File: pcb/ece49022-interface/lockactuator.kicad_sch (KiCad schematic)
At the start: 3 parts

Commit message: start pcb
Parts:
- MOSFET1: footprint SOT23_DMN3200U_2P9X1P3_DIO -> 49022_Footprints:SOT23_DMN3200U_2P9X1P3_DIO-L
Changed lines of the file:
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@@
 			)
 		)
-		(property "Footprint" "SOT23_DMN3200U_2P9X1P3_DIO"
+		(property "Footprint" "49022_Footprints:SOT23_DMN3200U_2P9X1P3_DIO-L"
 			(at 74.93 73.66 0)
 			(effects

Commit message: lock state
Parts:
- added L3: MSS1048T-563ML, symbol ECE49022_Symbols:MSS1048-103MLC
- added R11: R_US, symbol Device:R_US
- added R14: R_close, symbol Device:R_US
- added R7, R8: 10K, 1%, Resistor_SMD:R_0402_1005Metric_Pad0.72x0.64mm_HandSolder, symbol Device:R_US
- added SW2: SW_DPST_x2, symbol Switch:SW_DPST_x2
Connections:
- net +12V: now also R11.1
- net GND: now also R8.2
- net LOAD_RTN: now also L3.2
- new net: L3.1, R11.2
- new net: R14.1, SW2.2 (B)
- new net LOCK_GPIO_STATUS: R7.2, R8.1
- new net LOCK_STATUS: R14.2, R7.1
- new net LOCK_STATUS_VDD: SW2.1 (A)
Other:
- note added: "Equivalent Lock Circuit"
- moved on the sheet: D5, MOSFET1, R1

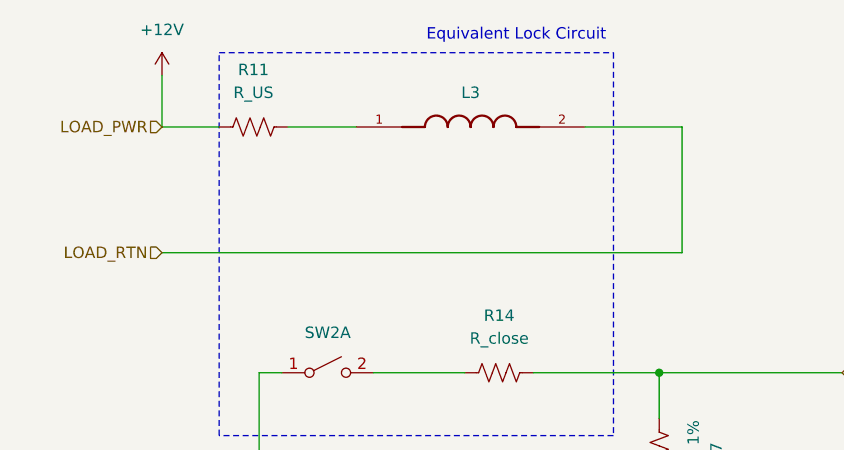
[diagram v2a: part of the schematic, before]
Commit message: update power resistors, wiring
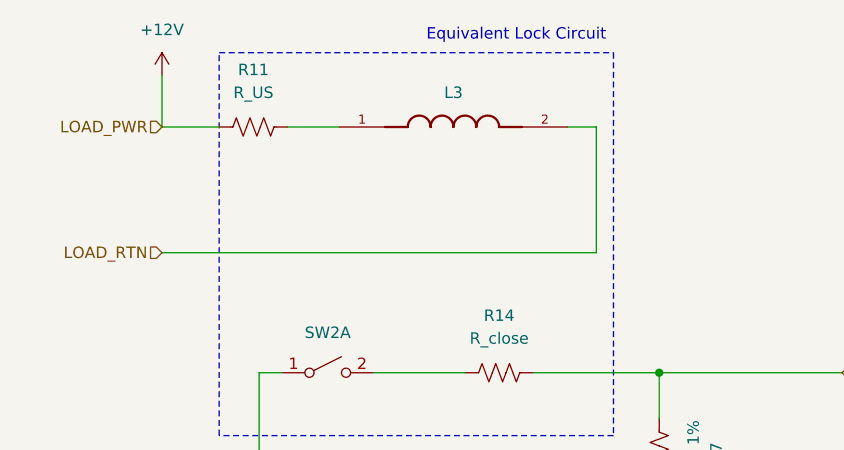
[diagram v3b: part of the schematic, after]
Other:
- moved on the sheet: L3
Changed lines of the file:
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@@
+	(wire
+		(pts
+			(xy 99.695 42.545) (xy 147.955 42.545)
+		)
+		(stroke
+			(width 0)
+			(type default)
+		)
+	)
 	(wire
 		(pts
@@
 	(wire
 		(pts
+			(xy 147.955 28.575) (xy 144.78 28.575)
+		)
+		(stroke
+			(width 0)
+			(type default)
+		)
+	)
+	(wire
+		(pts
 			(xy 57.15 105.41) (xy 57.15 106.68)
 		)
@@
 	(wire
 		(pts
-			(xy 157.48 28.575) (xy 157.48 42.545)
+			(xy 147.955 42.545) (xy 147.955 28.575)
 		)
 		(stroke
@@
 	(wire
 		(pts
+			(xy 113.665 28.575) (xy 119.38 28.575)
+		)
+		(stroke
+			(width 0)
+			(type default)
+		)
+	)
+	(wire
+		(pts
 			(xy 57.15 69.85) (xy 57.15 73.66)
 		)
@@
 	(wire
 		(pts
-			(xy 146.685 28.575) (xy 157.48 28.575)
-		)
-		(stroke
-			(width 0)
-			(type default)
-		)
-	)
-	(wire
-		(pts
 			(xy 154.94 68.58) (xy 154.94 73.66)
 		)
@@
 		(pts
 			(xy 45.72 105.41) (xy 57.15 105.41)
-		)
-		(stroke
-			(width 0)
-			(type default)
-		)
-	)
-	(wire
-		(pts
-			(xy 99.695 42.545) (xy 157.48 42.545)
-		)
-		(stroke
-			(width 0)
-			(type default)
-		)
-	)
-	(wire
-		(pts
-			(xy 113.665 28.575) (xy 121.285 28.575)
 		)
 		(stroke
@@
 	(symbol
 		(lib_id "ECE49022_Symbols:MSS1048-103MLC")
-		(at 133.985 28.575 0)
+		(at 132.08 28.575 0)
 		(unit 1)
 		(exclude_from_sim no)
@@
 		(dnp no)
 		(property "Reference" "L3"
-			(at 133.985 24.765 0)
+			(at 132.08 24.765 0)
 			(effects
 				(font
@@
 		)
 		(property "Value" "MSS1048T-563ML"
-			(at 133.985 24.765 0)
+			(at 132.08 24.765 0)
 			(effects
 				(font
@@
 		)
 		(property "Footprint" ""
-			(at 133.985 28.575 0)
+			(at 132.08 28.575 0)
 			(effects
 				(font
@@
 		)
 		(property "Datasheet" "https://www.coilcraft.com/getmedia/6f8116f7-0036-41bf-97c5-9bae06e6af25/mss1048t.pdf"
-			(at 133.985 28.575 0)
+			(at 132.08 28.575 0)
 			(effects
 				(font
@@
 		)
 		(property "Description" ""
-			(at 133.985 28.575 0)
+			(at 132.08 28.575 0)
 			(effects
 				(font
@@
 		)
 		(property "MF" "Coilcraft"
-			(at 133.731 20.447 0)
+			(at 131.826 20.447 0)
 			(effects
 				(font
@@
 		)
 		(property "MAXIMUM_PACKAGE_HEIGHT" "4.00mm"
-			(at 133.985 28.575 0)
+			(at 132.08 28.575 0)
 			(effects
 				(font
@@
 		)
 		(property "CREATOR" "AAMIR"
-			(at 133.985 28.575 0)
+			(at 132.08 28.575 0)
 			(effects
 				(font
@@
 		)
 		(property "Price" "None"
-			(at 133.985 28.575 0)
+			(at 132.08 28.575 0)
 			(effects
 				(font
@@
 		)
 		(property "Package" "None"
-			(at 133.985 28.575 0)
+			(at 132.08 28.575 0)
 			(effects
 				(font
@@
 		)
 		(property "Check_prices" "https://www.snapeda.com/parts/MSS1048-103MLC/Coilcraft/view-part/?ref=eda"
-			(at 133.731 23.749 0)
+			(at 131.826 23.749 0)
 			(effects
 				(font
@@
 		)
 		(property "STANDARD" "Manufacturer Recommendations"
-			(at 133.985 28.575 0)
+			(at 132.08 28.575 0)
 			(effects
 				(font
@@
 		)
 		(property "PARTREV" "02/16/22"
-			(at 133.985 28.575 0)
+			(at 132.08 28.575 0)
 			(effects
 				(font
@@
 		)
 		(property "VERIFIER" "RODRIGO"
-			(at 133.985 28.575 0)
+			(at 132.08 28.575 0)
 			(effects
 				(font
@@
 		)
 		(property "SnapEDA_Link" "https://www.snapeda.com/parts/MSS1048-103MLC/Coilcraft/view-part/?ref=snap"
-			(at 133.985 28.575 0)
+			(at 132.08 28.575 0)
 			(effects
 				(font
@@
 		)
 		(property "MP" "MSS1048-103MLC"
-			(at 133.985 28.575 0)
+			(at 132.08 28.575 0)
 			(effects
 				(font
@@
 		)
 		(property "Description_1" "10 µH Shielded Drum Core Inductor 4.79 A 23mOhm Max Nonstandard"
-			(at 133.985 28.575 0)
+			(at 132.08 28.575 0)
 			(effects
 				(font
@@
 		)
 		(property "Availability" "In Stock"
-			(at 133.985 28.575 0)
+			(at 132.08 28.575 0)
 			(effects
 				(font
@@
 		)
 		(property "MANUFACTURER" "Coilcraft"
-			(at 133.985 28.575 0)
-			(effects
-				(font
+			(at 132.08 28.575 0)
+			(effects
+				(font

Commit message: update
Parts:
- renumbered R14 to R15
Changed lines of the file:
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@@
 		(dnp no)
 		(fields_autoplaced yes)
-		(property "Reference" "R14"
+		(property "Reference" "R15"
 			(at 137.16 49.53 90)
 			(effects
@@
 			(project "ece49022-interface"
 				(path "/ad062fbe-cbe6-4ffd-876d-97a59a1c7176/2cda17de-48e9-4606-9fa0-f43b9c27831a"
-					(reference "R14")
+					(reference "R15")
 					(unit 1)
 				)
